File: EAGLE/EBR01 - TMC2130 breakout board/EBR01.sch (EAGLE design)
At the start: 27 parts

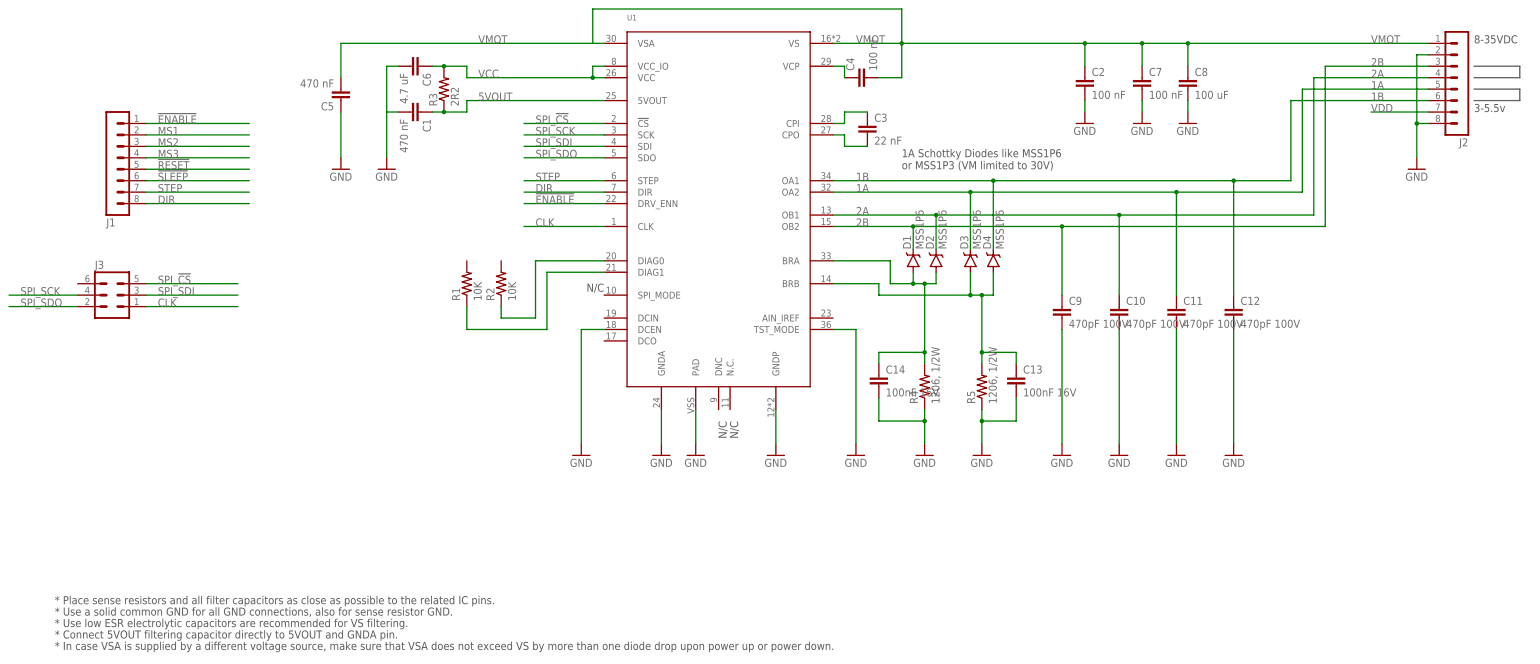
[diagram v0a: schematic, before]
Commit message: Have begun replacing placeholder components with TWT Library components. Cleaning up schematic in preparation for layout.
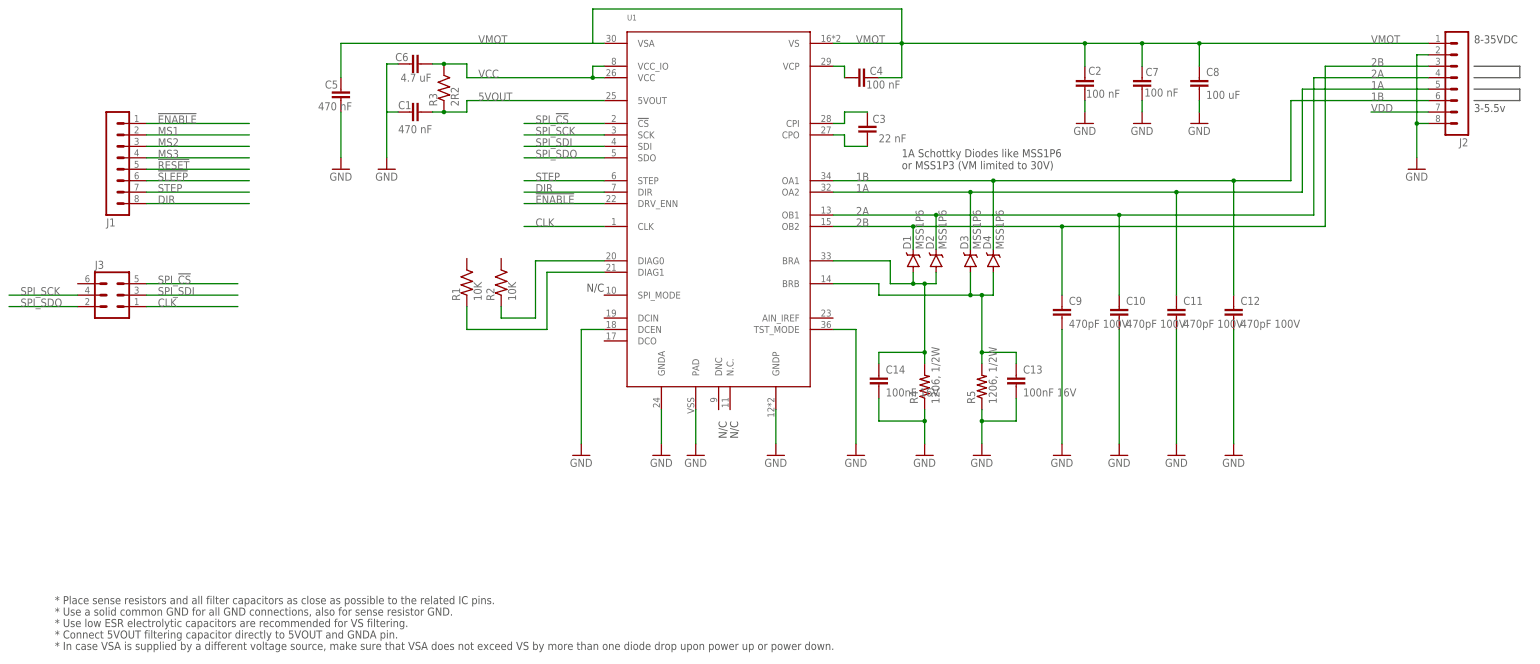
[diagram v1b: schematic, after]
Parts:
- C2, C4, C7: device SparkFun-Capacitors:CAP0603-CAP -> TinWhiskers:CPL-CAP-X7R-0603-100NF-50V
- C3: device SparkFun-Capacitors:CAP0603-CAP -> TinWhiskers:CPL-CAP-X7R-0603-22NF-50VKEMETC0603C223K5RAC
- C5: device SparkFun-Capacitors:CAP0603-CAP -> TinWhiskers:CPL-CAP-X7R-0603-470NF-16V
- C6: device SparkFun-Capacitors:CAP0603-CAP -> TinWhiskers:CPL-CAP-X5R-4.7UF-10V
- R1, R2: device SparkFun-Resistors:10KOHM-1/10W-1%(0603)0603 -> TinWhiskers:CPL-RES-0603-10K-0.1W
- R3: device SparkFun-Resistors:10KOHM-1/10W-1%(0603)0603 -> TinWhiskers:CPL-RES-0603-2.2-0.25W
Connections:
- net N$1: now also C3.2; no longer C3.1
- net N$5: now also C3.1; no longer C3.2
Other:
- moved on the sheet: C6, C8

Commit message: Updated all components to reflect accurate devices. Smashed most of the parts that required it. The only remaining issues with the schematic are the external voltage regulator and a couple unconnected connections which require clarification.
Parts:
- removed C8: 100 uF, SparkFun-Capacitors:CAP0603-CAP
- removed R1, R2: 10K, TinWhiskers:CPL-RES-0603-10K-0.1W
- C10, C11, C12, C9: value 470pF 100V -> 470pF; device SparkFun-Capacitors:CAP0603-CAP -> TinWhiskers:CPL-CAP-X7R-0603-470PF-100V
- C13, C14: value 100nF 16V -> 100nF; device SparkFun-Capacitors:CAP0603-CAP -> TinWhiskers:CPL-CAP-X7R-0603-100NF-50V
- D1, D2, D3, D4: device SparkFun-DiscreteSemi:DIODE-SCHOTTKY-BAT20J -> TinWhiskers:CPL-DIO-MSS1P6-MICROSMP
- J1, J2: value (none) -> CPL-CON-HEADER-0.1IN-8P-M; device !con-lstb:MA08-1 -> TinWhiskers:CPL-CON-HEADER-0.1IN-8P-M
- J3: value (none) -> CPL-CON-HEADER-0.1IN-2X3P-M; device !con-lstb:MA03-2 -> TinWhiskers:CPL-CON-HEADER-0.1IN-2X3P-M
- R4, R5: value 1206, 1/2W -> 0.22; device SparkFun-Resistors:10KOHM-1/10W-1%(0603)0603 -> TinWhiskers:CPL-RES-1206-0.22-0.5W
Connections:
- removed net N$6: R2.1, U1.DIAG0
- removed net N$7: R1.1, U1.DIAG1
- net GND: no longer C8.2
- net VMOT: no longer C8.1
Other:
- moved on the sheet: C1, C10, C11, C12, C6, C9, R3
